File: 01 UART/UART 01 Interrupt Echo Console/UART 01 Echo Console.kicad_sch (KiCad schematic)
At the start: 22 parts, among them J101 ICSP, J102 USB_A, J103 DE9_Pins, U101 PIC18F47Q43-I/PT, U102 MAX232, U103 FT232RL

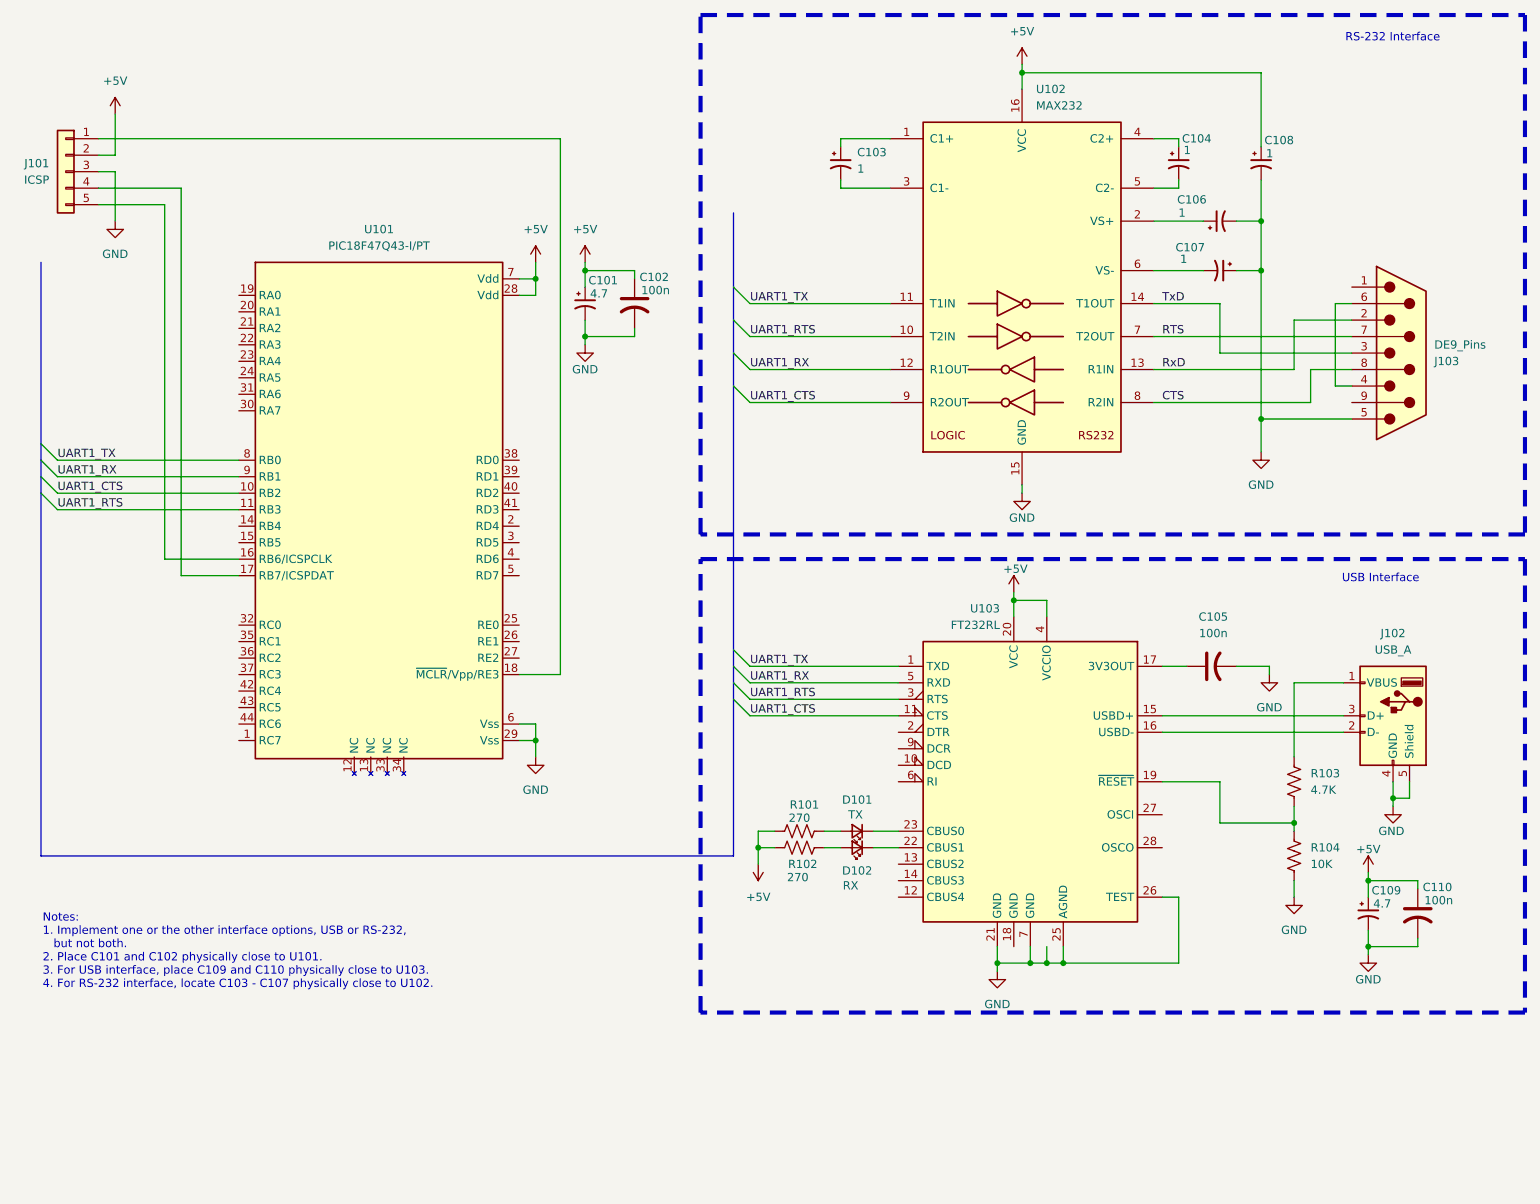
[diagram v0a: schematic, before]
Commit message: transmit and receive are working
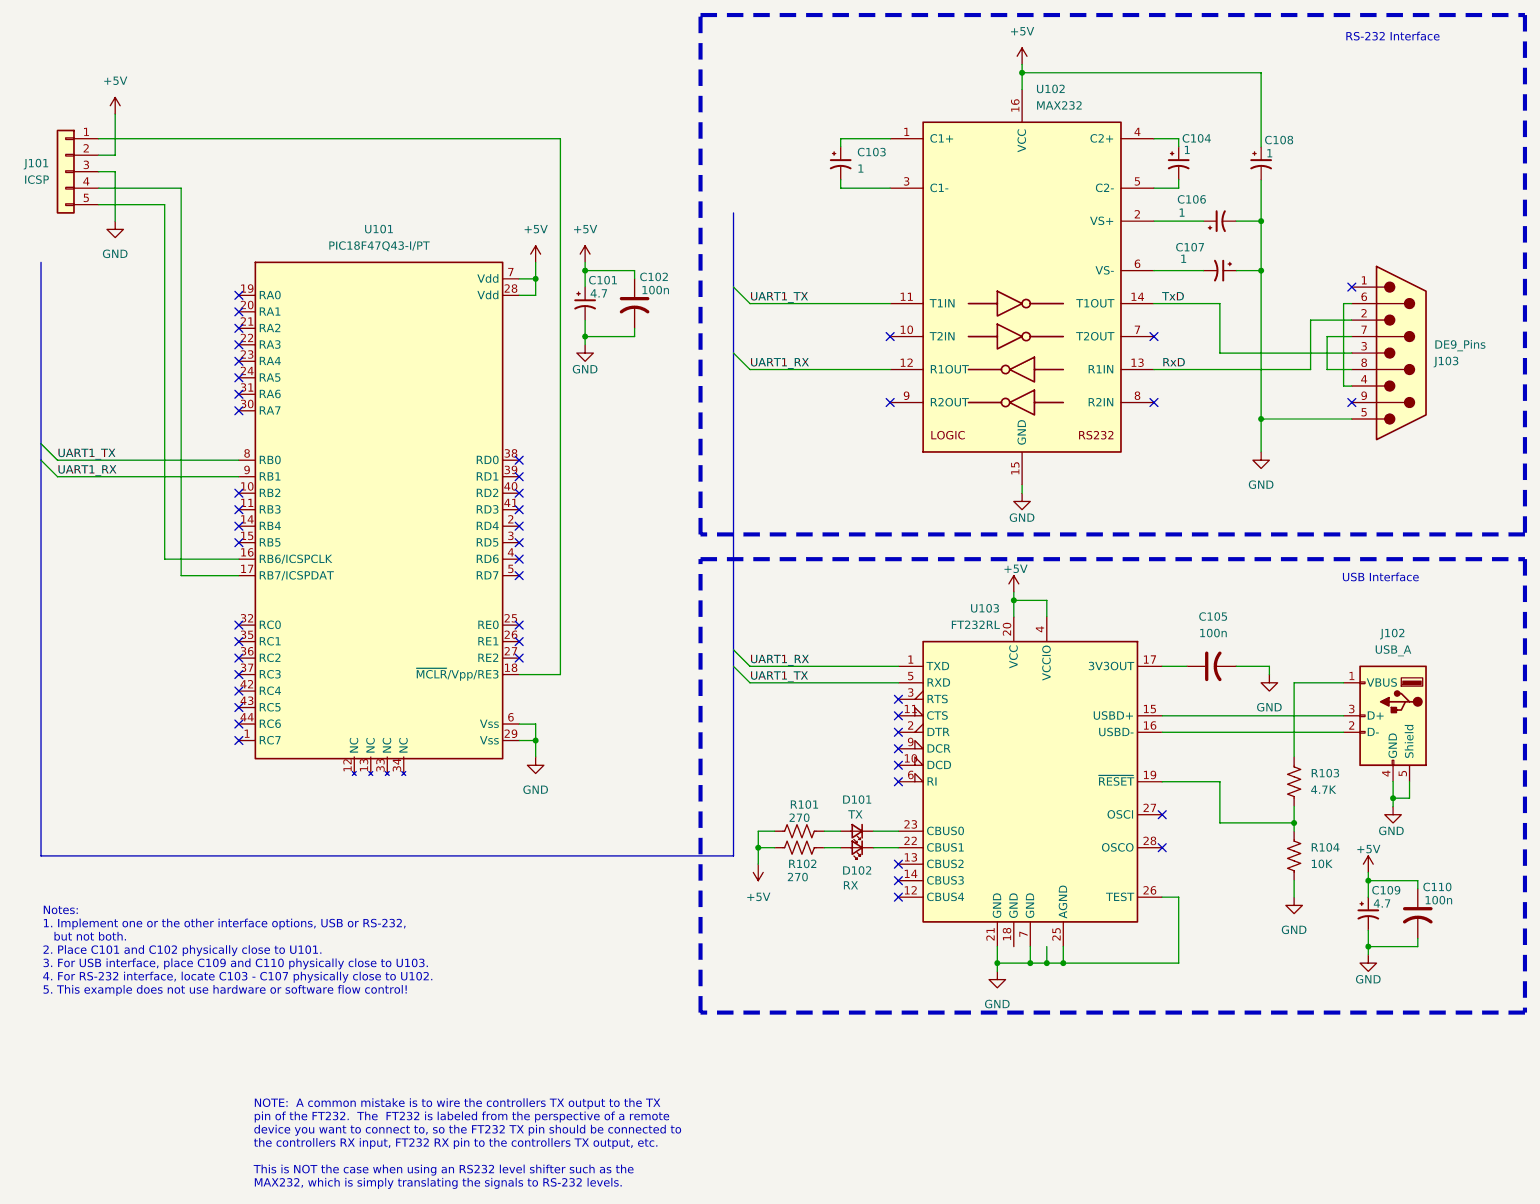
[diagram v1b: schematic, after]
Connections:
- net UART1_RX: now also U103.1 (TXD); no longer U103.5 (RXD)
- net UART1_TX: now also U103.5 (RXD); no longer U103.1 (TXD)
- net CTS: no longer names the net of U102.8 (R2IN)
- net CTS: no longer J103.8
- net RTS: no longer names the net of U102.7 (T2OUT)
- net RTS: no longer J103.7
- removed net UART1_CTS: U101.10 (RB2), U102.9 (R2OUT), U103.11 (CTS)
- removed net UART1_RTS: U101.11 (RB3), U102.10 (T2IN), U103.3 (RTS)
- new net: J103.7, J103.8
- no-connect marks 0 -> 48
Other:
- note added: "NOTE: A common mistake is to wire the controllers TX output to the TX pin of the FT232. The FT232 is labeled from the perspective of a remote device you want to connect to, so the FT232 TX pin should be connected to the controllers RX input, FT232 RX pin to the controllers TX output, etc. This is NOT the case when using an RS232 level shifter such as the MAX232, which is simply translating the si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"
- note added: "Notes: 1. Implement one or the other interface options, USB or RS-232, but not both. 2. Place C101 and C102 physically close to U101. 3. For USB interface, place C109 and C110 physically close to U103. 4. For RS-232 interface, locate C103 - C107 physically close to U102. 5. This example does not use hardware or software flow control!"
- note removed: "Notes: 1. Implement one or the other interface options, USB or RS-232, but not both. 2. Place C101 and C102 physically close to U101. 3. For USB interface, place C109 and C110 physically close to U103. 4. For RS-232 interface, locate C103 - C107 physically close to U102."
